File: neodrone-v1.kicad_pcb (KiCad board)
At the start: 4 copper layers, 150 x 105 mm, 39 parts, among them J1 Conn_01x05_Socket, U1 ATSAMD21G18A-A, U2 MPU-6000

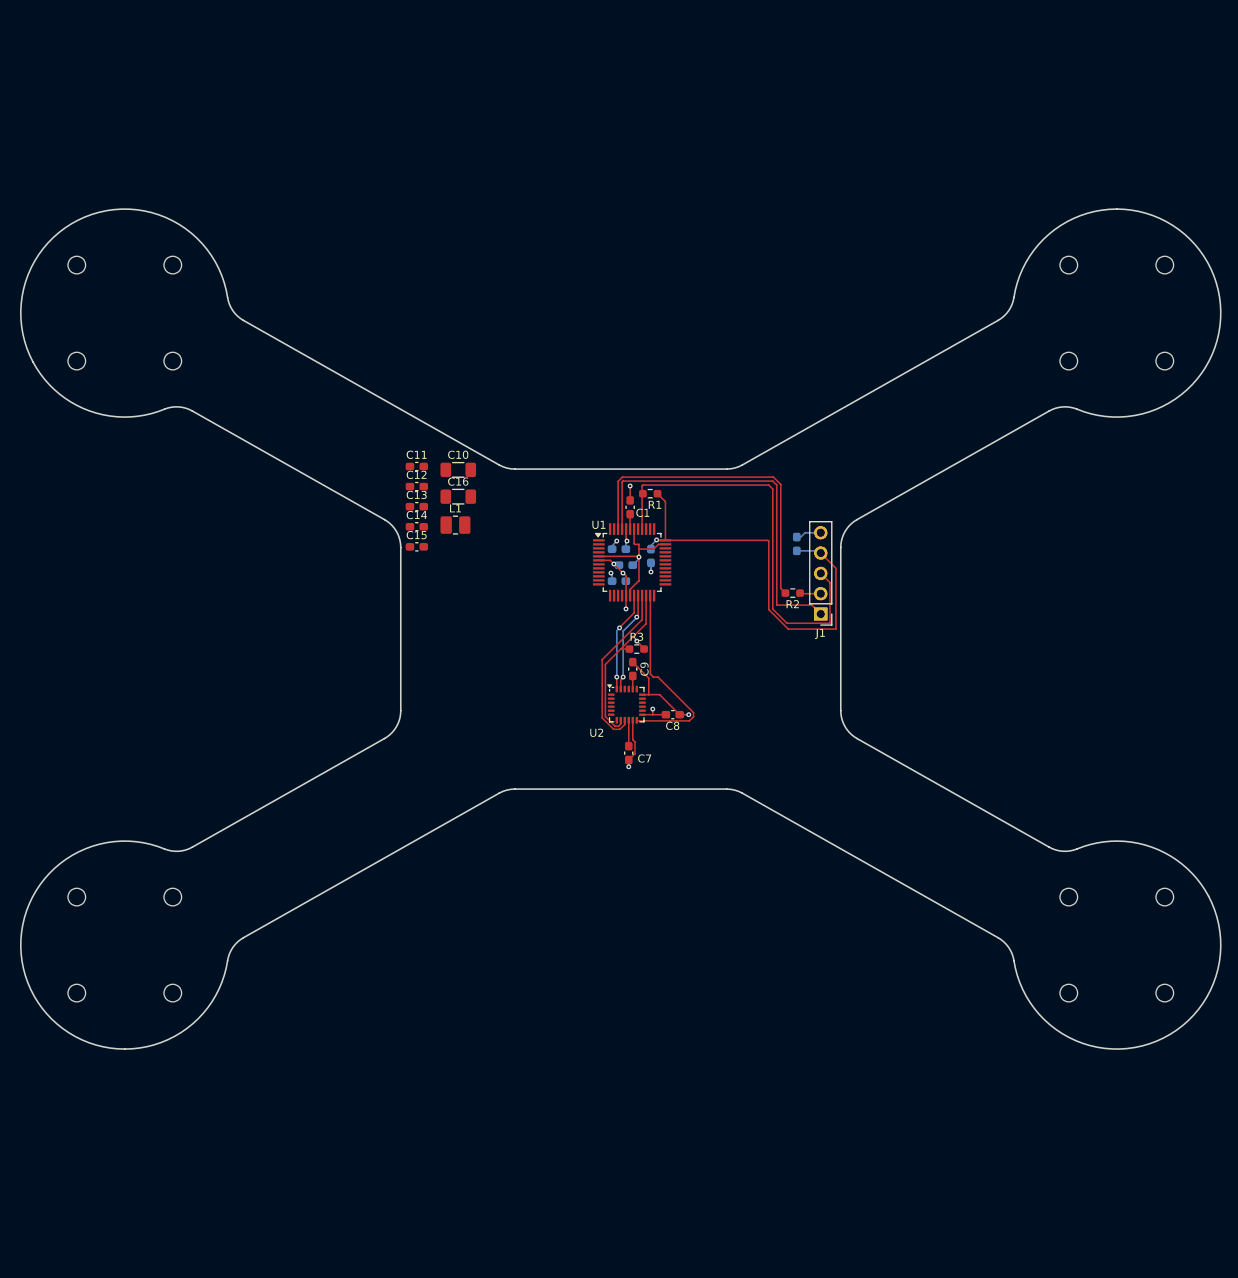
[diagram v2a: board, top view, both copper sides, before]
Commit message: Schematics mostly done, netclasses, coords for esc (angled)
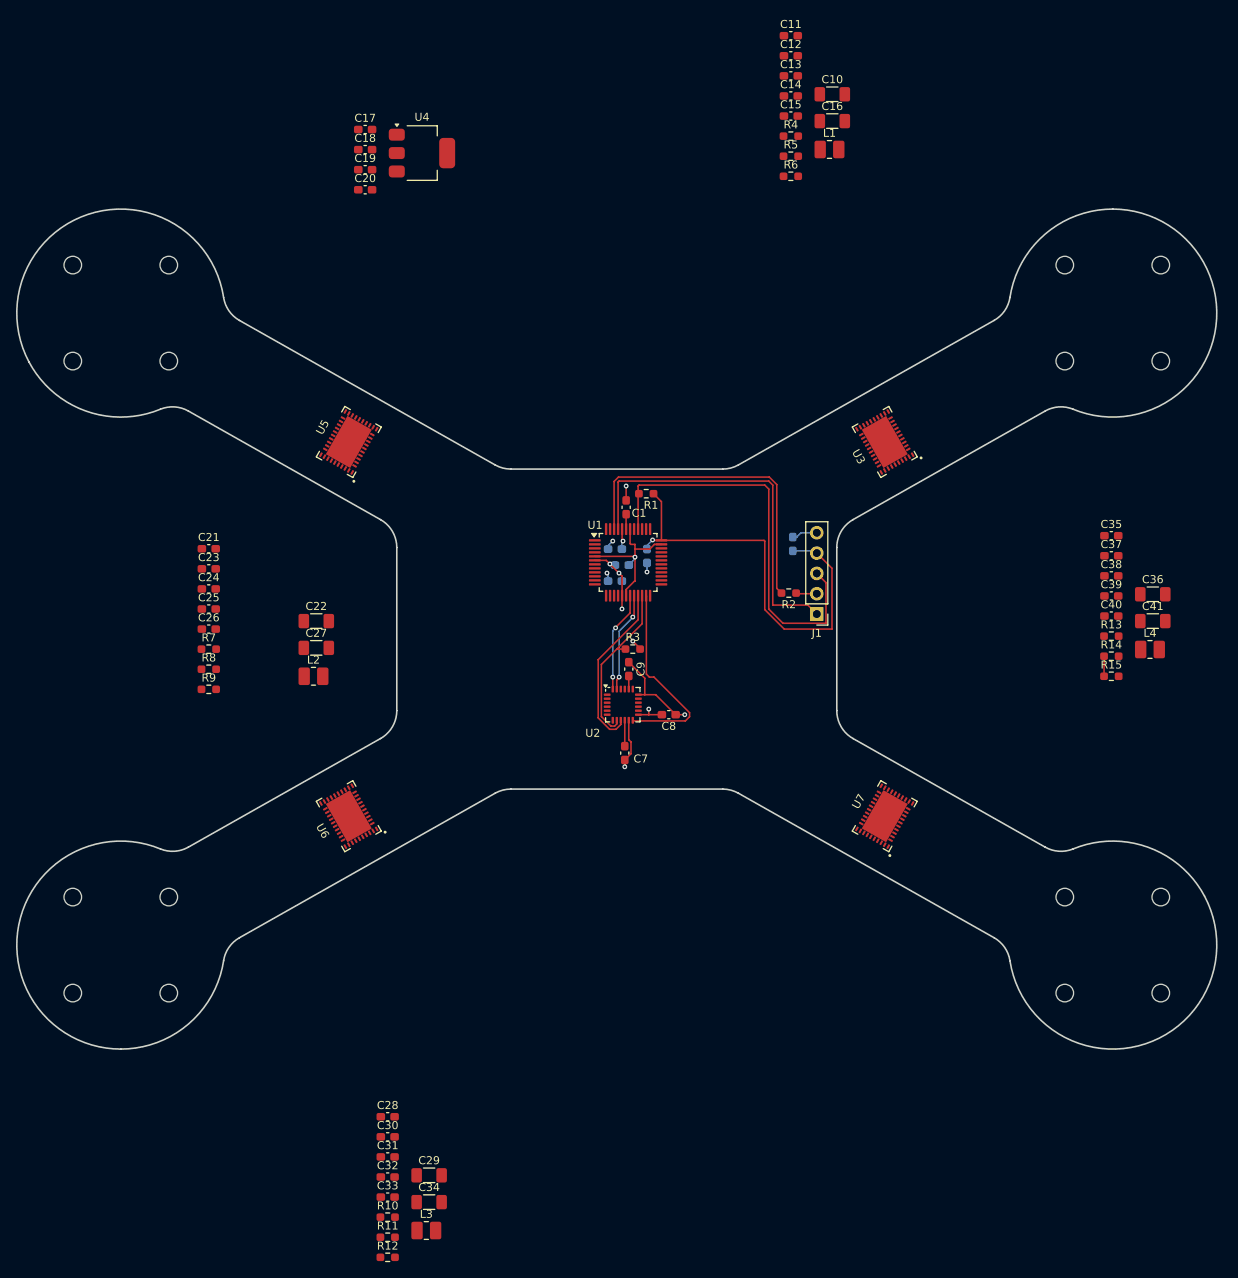
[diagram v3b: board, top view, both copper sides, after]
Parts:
- added C17: 100nF, Capacitor_SMD:C_0603_1608Metric_Pad1.08x0.95mm_HandSolder, F.Cu at (118.5, 37.6)
- added C18: 10uF, Capacitor_SMD:C_0603_1608Metric_Pad1.08x0.95mm_HandSolder, F.Cu at (118.5, 40.1)
- added C19: 100nF, Capacitor_SMD:C_0603_1608Metric_Pad1.08x0.95mm_HandSolder, F.Cu at (118.5, 42.6)
- added C20: 10uF, Capacitor_SMD:C_0603_1608Metric_Pad1.08x0.95mm_HandSolder, F.Cu at (118.5, 45.1)
- added C21: 100nF, Capacitor_SMD:C_0603_1608Metric_Pad1.08x0.95mm_HandSolder, F.Cu at (99.0, 90.0)
- added C22: 22uF, Capacitor_SMD:C_1206_3216Metric_Pad1.33x1.80mm_HandSolder, F.Cu at (112.4, 99.0)
- added C23: 1uF, Capacitor_SMD:C_0603_1608Metric_Pad1.08x0.95mm_HandSolder, F.Cu at (99.0, 92.5)
- added C24: 1uF, Capacitor_SMD:C_0603_1608Metric_Pad1.08x0.95mm_HandSolder, F.Cu at (99.0, 95.0)
- added C25: 1uF, Capacitor_SMD:C_0603_1608Metric_Pad1.08x0.95mm_HandSolder, F.Cu at (99.0, 97.5)
- added C26: 47nF, Capacitor_SMD:C_0603_1608Metric_Pad1.08x0.95mm_HandSolder, F.Cu at (99.0, 100.0)
- added C27: 22uF, Capacitor_SMD:C_1206_3216Metric_Pad1.33x1.80mm_HandSolder, F.Cu at (112.4, 102.3)
- added C28: 100nF, Capacitor_SMD:C_0603_1608Metric_Pad1.08x0.95mm_HandSolder, F.Cu at (121.4, 161.0)
- added C29: 22uF, Capacitor_SMD:C_1206_3216Metric_Pad1.33x1.80mm_HandSolder, F.Cu at (126.5, 168.3)
- added C30: 1uF, Capacitor_SMD:C_0603_1608Metric_Pad1.08x0.95mm_HandSolder, F.Cu at (121.4, 163.5)
- added C31: 1uF, Capacitor_SMD:C_0603_1608Metric_Pad1.08x0.95mm_HandSolder, F.Cu at (121.4, 166.0)
- added C32: 1uF, Capacitor_SMD:C_0603_1608Metric_Pad1.08x0.95mm_HandSolder, F.Cu at (121.4, 168.5)
- added C33: 47nF, Capacitor_SMD:C_0603_1608Metric_Pad1.08x0.95mm_HandSolder, F.Cu at (121.4, 171.0)
- added C34: 22uF, Capacitor_SMD:C_1206_3216Metric_Pad1.33x1.80mm_HandSolder, F.Cu at (126.5, 171.6)
- added C35: 100nF, Capacitor_SMD:C_0603_1608Metric_Pad1.08x0.95mm_HandSolder, F.Cu at (211.8, 88.3)
- added C36: 22uF, Capacitor_SMD:C_1206_3216Metric_Pad1.33x1.80mm_HandSolder, F.Cu at (217.0, 95.7)
- added C37: 1uF, Capacitor_SMD:C_0603_1608Metric_Pad1.08x0.95mm_HandSolder, F.Cu at (211.8, 90.8)
- added C38: 1uF, Capacitor_SMD:C_0603_1608Metric_Pad1.08x0.95mm_HandSolder, F.Cu at (211.8, 93.3)
- added C39: 1uF, Capacitor_SMD:C_0603_1608Metric_Pad1.08x0.95mm_HandSolder, F.Cu at (211.8, 95.9)
- added C40: 47nF, Capacitor_SMD:C_0603_1608Metric_Pad1.08x0.95mm_HandSolder, F.Cu at (211.8, 98.4)
- added C41: 22uF, Capacitor_SMD:C_1206_3216Metric_Pad1.33x1.80mm_HandSolder, F.Cu at (217.0, 99.0)
- added L2: 2.2uH, Inductor_SMD:L_1008_2520Metric_Pad1.43x2.20mm_HandSolder, F.Cu at (112.1, 105.9)
- added L3: 2.2uH, Inductor_SMD:L_1008_2520Metric_Pad1.43x2.20mm_HandSolder, F.Cu at (126.2, 175.2)
- added L4: 2.2uH, Inductor_SMD:L_1008_2520Metric_Pad1.43x2.20mm_HandSolder, F.Cu at (216.7, 102.5)
- added R10: 10k, Resistor_SMD:R_0603_1608Metric_Pad0.98x0.95mm_HandSolder, F.Cu at (121.4, 173.5)
- added R11: 10k, Resistor_SMD:R_0603_1608Metric_Pad0.98x0.95mm_HandSolder, F.Cu at (121.4, 176.0)
- added R12: 10k, Resistor_SMD:R_0603_1608Metric_Pad0.98x0.95mm_HandSolder, F.Cu at (121.4, 178.5)
- added R13: 10k, Resistor_SMD:R_0603_1608Metric_Pad0.98x0.95mm_HandSolder, F.Cu at (211.8, 100.9)
- added R14: 10k, Resistor_SMD:R_0603_1608Metric_Pad0.98x0.95mm_HandSolder, F.Cu at (211.8, 103.4)
- added R15: 10k, Resistor_SMD:R_0603_1608Metric_Pad0.98x0.95mm_HandSolder, F.Cu at (211.8, 105.9)
- added R4: 10k, Resistor_SMD:R_0603_1608Metric_Pad0.98x0.95mm_HandSolder, F.Cu at (171.8, 38.4)
- added R5: 10k, Resistor_SMD:R_0603_1608Metric_Pad0.98x0.95mm_HandSolder, F.Cu at (171.8, 40.9)
- added R6: 10k, Resistor_SMD:R_0603_1608Metric_Pad0.98x0.95mm_HandSolder, F.Cu at (171.8, 43.4)
- added R7: 10k, Resistor_SMD:R_0603_1608Metric_Pad0.98x0.95mm_HandSolder, F.Cu at (99.0, 102.5)
- added R8: 10k, Resistor_SMD:R_0603_1608Metric_Pad0.98x0.95mm_HandSolder, F.Cu at (99.0, 105.0)
- added R9: 10k, Resistor_SMD:R_0603_1608Metric_Pad0.98x0.95mm_HandSolder, F.Cu at (99.0, 107.5)
- added U3: MCF8316A, MCF8316:MCF8316A_RGF0040E_VQFN-40-1EP_7x5mm_P0.5mm_EP5.5x3.5mm_kicad5_fixed_rotation, F.Cu at (183.5, 76.6)
- added U4: MCP1826S, Package_TO_SOT_SMD:SOT-223-3_TabPin2, F.Cu at (125.7, 40.5)
- added U5: MCF8316A, MCF8316:MCF8316A_RGF0040E_VQFN-40-1EP_7x5mm_P0.5mm_EP5.5x3.5mm_kicad5_fixed_rotation, F.Cu at (116.5, 76.6)
- added U6: MCF8316A, MCF8316:MCF8316A_RGF0040E_VQFN-40-1EP_7x5mm_P0.5mm_EP5.5x3.5mm_kicad5_fixed_rotation, F.Cu at (116.5, 123.4)
- added U7: MCF8316A, MCF8316:MCF8316A_RGF0040E_VQFN-40-1EP_7x5mm_P0.5mm_EP5.5x3.5mm_kicad5_fixed_rotation, F.Cu at (183.5, 123.4)
- moved C11 71.3 mm to (171.8, 25.8)
- moved C13 71.3 mm to (171.8, 30.9)
- moved C15 71.3 mm to (171.8, 35.9)
- moved C12 71.3 mm to (171.8, 28.3)
- moved C14 71.3 mm to (171.8, 33.4)
- moved C10 66.3 mm to (176.9, 33.1)
- moved C16 66.3 mm to (176.9, 36.5)
- moved L1 66.3 mm to (176.6, 40.0)
- moved R1 0.50 mm to (153.7, 83.1)
- moved C8 0.50 mm to (156.5, 110.7)
- moved M10 0.50 mm to (82.0, 133.5)
- moved M11 0.50 mm to (82.0, 145.5)
- moved M12 0.50 mm to (94.0, 145.5)
- moved M5 0.50 mm to (94.0, 54.5)
- moved M6 0.50 mm to (82.0, 54.5)
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- renumbered REF** to M1, REF** to M10, REF** to M11, REF** to M12, REF** to M13, REF** to M14, REF** to M15, REF** to M16, REF** to M2, REF** to M3, REF** to M4, REF** to M5, REF** to M6, REF** to M7, REF** to M8, REF** to M9
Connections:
- net /motor_esc/PGND_M1 renamed /motor_esc1/PGND_M1
- net /motor_esc/VBAT renamed /motor_esc1/VBAT
- net /motor_esc/VBK_M1 renamed VBK_M1
- C16 pad 2: /motor_esc/GND_BK_M1 -> GND_BK_M1
- U1 pad 13: /mcu/I2C_SDA -> unconnected-(U1-PA08-Pad13)
- U1 pad 14: /mcu/I2C_SCL -> unconnected-(U1-PA09-Pad14)
- U1 pad 25: /mcu/M1_PWM -> M1_PWM
- U1 pad 26: /mcu/M2_PWM -> M2_PWM
- U1 pad 27: /mcu/M3_PWM -> M3_PWM
- U1 pad 28: /mcu/M4_PWM -> M4_PWM
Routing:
- net Net-(U7-AGND): track 0.00 -> 2.51 mm
- net +3V3: track 93.5 -> 95.1 mm
- net GND: track 45.7 -> 46.9 mm

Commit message: A LOT of changes, current state is 2 of 4 ESCs routed, power revamped. \n Board almost done
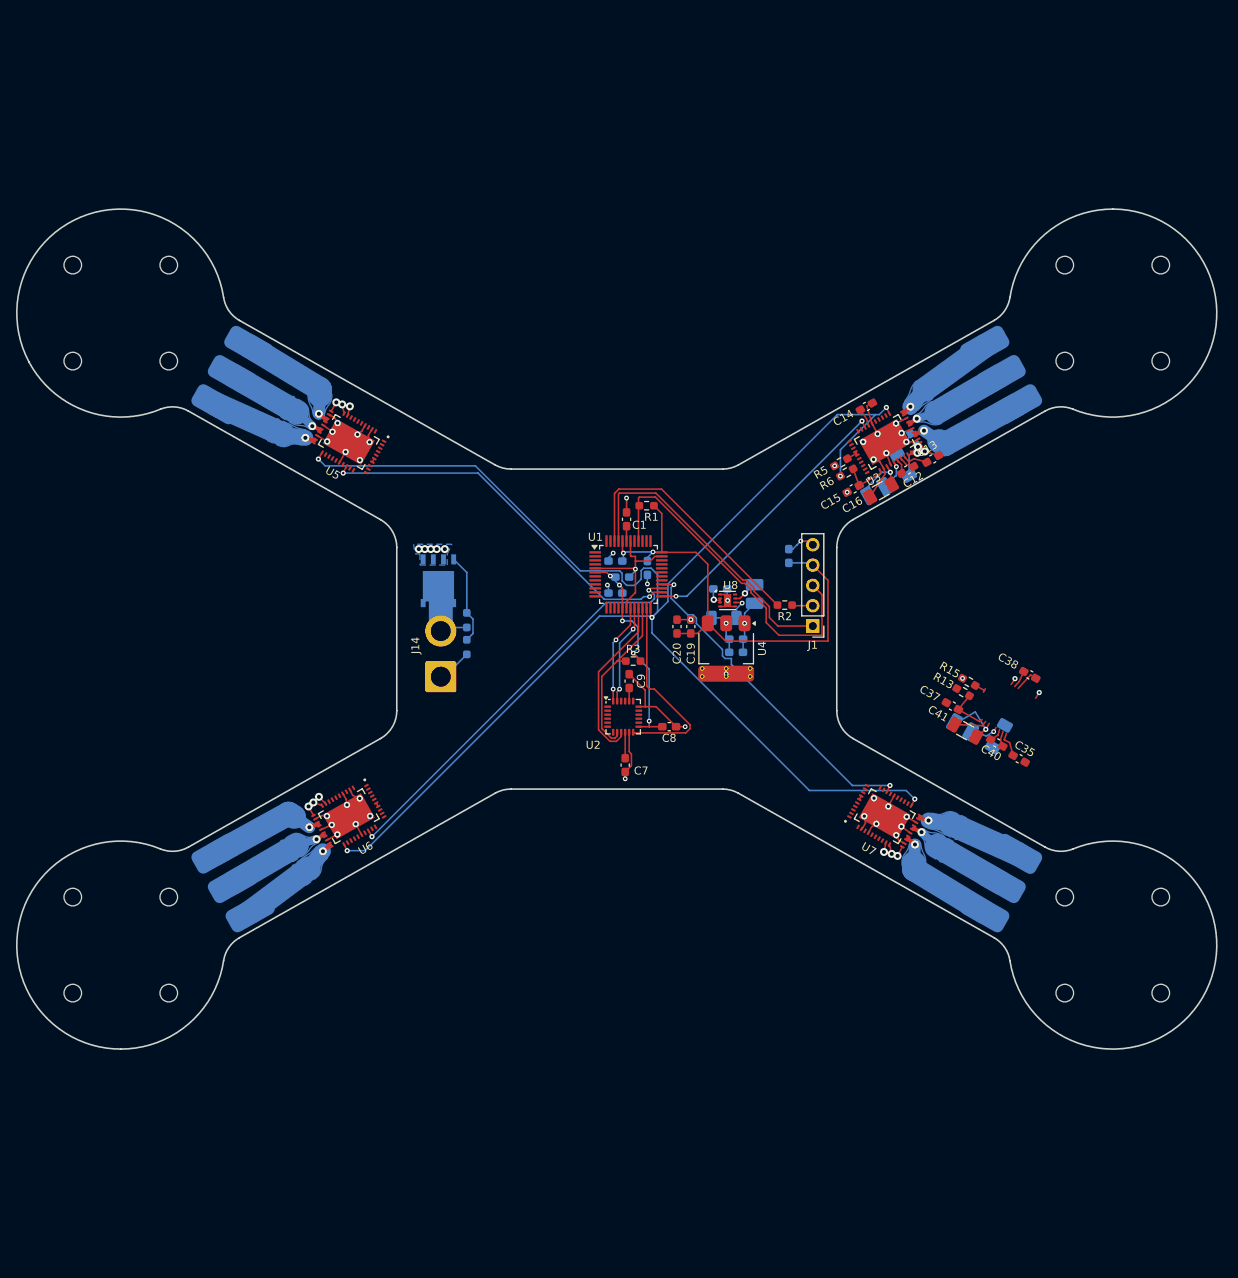
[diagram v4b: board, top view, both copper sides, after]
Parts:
- removed the C10 at (176.9, 33.1)
- removed C21, C28: 100nF, Capacitor_SMD:C_0603_1608Metric_Pad1.08x0.95mm_HandSolder
- removed C22, C27, C29, C34, C36: 22uF, Capacitor_SMD:C_1206_3216Metric_Pad1.33x1.80mm_HandSolder
- removed C23, C24, C25, C30, C31, C32, C39: 1uF, Capacitor_SMD:C_0603_1608Metric_Pad1.08x0.95mm_HandSolder
- removed C26, C33: 47nF, Capacitor_SMD:C_0603_1608Metric_Pad1.08x0.95mm_HandSolder
- removed L2, L3: 2.2uH, Inductor_SMD:L_1008_2520Metric_Pad1.43x2.20mm_HandSolder
- removed R10, R11, R12, R14, R4, R7, R8, R9: 10k, Resistor_SMD:R_0603_1608Metric_Pad0.98x0.95mm_HandSolder
- added C10: 22uF, Capacitor_SMD:C_1206_3216Metric_Pad1.33x1.80mm_HandSolder, B.Cu at (185.8, 79.5)
- added C10: 22uF, Capacitor_SMD:C_1206_3216Metric_Pad1.33x1.80mm_HandSolder, B.Cu at (197.7, 113.4)
- added C42: 10uF, Capacitor_SMD:C_0603_1608Metric_Pad1.08x0.95mm_HandSolder, B.Cu at (162.9, 95.0)
- added C43: 22uF, Capacitor_SMD:C_1206_3216Metric_Pad1.33x1.80mm_HandSolder, B.Cu at (163.4, 98.6)
- added J10: SolderWirePad_1x01_SMD_3x6mm, Connector_Wire:SolderWirePad_1x01_SMD_3x6mm, B.Cu at (104.2, 135.4)
- added J11: SolderWirePad_1x01_SMD_3x6mm, Connector_Wire:SolderWirePad_1x01_SMD_3x6mm, B.Cu at (196.0, 135.4)
- added J12: SolderWirePad_1x01_SMD_3x6mm, Connector_Wire:SolderWirePad_1x01_SMD_3x6mm, B.Cu at (198.1, 131.8)
- added J13: SolderWirePad_1x01_SMD_3x6mm, Connector_Wire:SolderWirePad_1x01_SMD_3x6mm, B.Cu at (200.1, 128.1)
- added J14: Conn_01x02, Connector_Wire:SolderWire-2sqmm_1x02_P7.8mm_D2mm_OD3.9mm, F.Cu at (128.0, 106.0)
- added J2: SolderWirePad_1x01_SMD_3x6mm, Connector_Wire:SolderWirePad_1x01_SMD_3x6mm, B.Cu at (200.1, 71.9)
- added J3: SolderWirePad_1x01_SMD_3x6mm, Connector_Wire:SolderWirePad_1x01_SMD_3x6mm, B.Cu at (198.1, 68.2)
- added J4: SolderWirePad_1x01_SMD_3x6mm, Connector_Wire:SolderWirePad_1x01_SMD_3x6mm, B.Cu at (196.0, 64.6)
- added J5: SolderWirePad_1x01_SMD_3x6mm, Connector_Wire:SolderWirePad_1x01_SMD_3x6mm, B.Cu at (104.0, 64.6)
- added J6: SolderWirePad_1x01_SMD_3x6mm, Connector_Wire:SolderWirePad_1x01_SMD_3x6mm, B.Cu at (102.0, 68.2)
- added J7: SolderWirePad_1x01_SMD_3x6mm, Connector_Wire:SolderWirePad_1x01_SMD_3x6mm, B.Cu at (99.9, 71.9)
- added J8: SolderWirePad_1x01_SMD_3x6mm, Connector_Wire:SolderWirePad_1x01_SMD_3x6mm, B.Cu at (99.9, 128.1)
- added J9: SolderWirePad_1x01_SMD_3x6mm, Connector_Wire:SolderWirePad_1x01_SMD_3x6mm, B.Cu at (102.0, 131.8)
- added L5: 2.2uH, Inductor_SMD:L_1008_2520Metric_Pad1.43x2.20mm_HandSolder, B.Cu at (167.2, 95.6)
- added Q1: Si7139DP, Package_SO:PowerPAK_SO-8_Single, B.Cu at (127.7, 94.0)
- added R16: 100k, Resistor_SMD:R_0603_1608Metric_Pad0.98x0.95mm_HandSolder, B.Cu at (131.2, 98.9)
- added R17: 100k, Resistor_SMD:R_0603_1608Metric_Pad0.98x0.95mm_HandSolder, B.Cu at (131.2, 102.2)
- added U8: TPS62163DSG, Package_SON:WSON-8-1EP_2x2mm_P0.5mm_EP0.9x1.6mm, F.Cu at (163.8, 96.4)
- C11, C17, C18, L1, L4: moved to B.Cu
- C35: value 100nF -> 1uF
- U3, U5, U6, U7: footprint MCF8316:MCF8316A_RGF0040E_VQFN-40-1EP_7x5mm_P0.5mm_EP5.5x3.5mm_kicad5_fixed_rotation -> MCF8316:MCF8316A_RGF0040E_VQFN-40-1EP_7x5mm_P0.5mm_EP5.5x3.5mm
- moved C17 78.8 mm to (164.9, 101.2), turned to 180 degrees
- moved C18 78.1 mm to (164.9, 102.9)
- moved U4 72.7 mm to (163.7, 102.4), turned to -90 degrees
- moved C19 70.1 mm to (159.2, 99.7), turned to 90 degrees
- moved C20 67.1 mm to (157.5, 99.7), turned to -90 degrees
- moved C12 53.8 mm to (186.3, 80.1), turned to -150.524 degrees
- moved C11 52.8 mm to (187.2, 76.3), turned to 119.476 degrees
- moved C13 51.1 mm to (189.5, 78.7), turned to 29.476 degrees
- moved C15 47.3 mm to (179.6, 82.5), turned to -150.524 degrees
- moved C16 46.6 mm to (183.0, 82.7), turned to -150.524 degrees
- moved L1 43.1 mm to (182.5, 82.8), turned to -150.524 degrees
- moved C14 39.9 mm to (181.2, 72.2), turned to 29.476 degrees
- moved R5 38.8 mm to (178.0, 79.2), turned to 29.476 degrees
- moved R6 37.7 mm to (178.8, 80.4), turned to -150.524 degrees
- moved C35 30.2 mm to (200.3, 116.2), turned to -29.4758 degrees
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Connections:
- C11 pad 1: /motor_esc1/VBAT -> VBAT
- C11 pad 2: /motor_esc1/PGND_M1 -> GND
- C13 pad 2: /motor_esc1/VBAT -> VBAT
- C14 pad 2: Net-(U3-AGND) -> GND
- C15 pad 2: Net-(U3-DGND) -> GND
- C16 pad 2: GND_BK_M1 -> GND
- C17 pad 1: VBK_M1 -> Net-(U4-VI)
- C17 pad 2: GND_BK_M1 -> GND
- C18 pad 1: GND_BK_M1 -> GND
- C18 pad 2: VBK_M1 -> Net-(U4-VI)
- C19 pad 2: GND_BK_M1 -> GND
- C20 pad 1: GND_BK_M1 -> GND
- C35 pad 1: /motor_esc4/VBAT -> Net-(U3-CP)
- C35 pad 2: /motor_esc4/PGND_M4 -> VBAT
- C37 pad 1: Net-(U7-DVDD) -> Net-(U3-DVDD)
- C37 pad 2: Net-(U7-DGND) -> GND
- C38 pad 1: Net-(U7-AVDD) -> Net-(U3-AVDD)
- C38 pad 2: Net-(U7-AGND) -> GND
- C40 pad 1: Net-(U7-CPH) -> Net-(U3-CPH)
- C40 pad 2: Net-(U7-CPL) -> Net-(U3-CPL)
- C41 pad 2: GND_BK_M4 -> GND
- R13 pad 1: Net-(U7-AVDD) -> Net-(U3-DVDD)
- R15 pad 1: Net-(U7-AGND) -> GND
- R15 pad 2: Net-(U7-BRAKE) -> Net-(U3-BRAKE)
- R5 pad 1: Net-(U3-AGND) -> GND
- R6 pad 1: Net-(U3-AVDD) -> Net-(U3-DVDD)
- U1 pad 24: unconnected-(U1-PA15-Pad24) -> DRVOFF_ALL
- U3 pad 10: /motor_esc1/VBAT -> VBAT
- U3 pad 11: /motor_esc1/VBAT -> VBAT
- U3 pad 12: /motor_esc1/PGND_M1 -> GND
- U3 pad 15: /motor_esc1/PGND_M1 -> GND
- U3 pad 18: /motor_esc1/PGND_M1 -> GND
- U3 pad 2: Net-(U3-DGND) -> GND
- U3 pad 26: Net-(U3-AGND) -> GND
- U3 pad 34: Net-(U3-DIR) -> Net-(U3-BRAKE)
- U3 pad 4: GND_BK_M1 -> GND
- U3 pad 41: /motor_esc1/PGND_M1 -> GND
- U3 pad 9: /motor_esc1/VBAT -> VBAT
- U4 pad 1: VBK_M1 -> Net-(U4-VI)
- U4 pad 2: GND_BK_M1 -> GND
- U5 pad 10: /motor_esc2/VBAT -> VBAT
- U5 pad 11: /motor_esc2/VBAT -> VBAT
- U5 pad 12: /motor_esc2/PGND_M2 -> GND
- U5 pad 15: /motor_esc2/PGND_M2 -> GND
- U5 pad 18: /motor_esc2/PGND_M2 -> GND
- U5 pad 2: Net-(U5-DGND) -> GND
- U5 pad 26: Net-(U5-AGND) -> GND
- U5 pad 34: Net-(U5-DIR) -> Net-(U5-BRAKE)
- U5 pad 4: GND_BK_M2 -> GND
- U5 pad 41: /motor_esc2/PGND_M2 -> GND
- U5 pad 9: /motor_esc2/VBAT -> VBAT
- U6 pad 10: /motor_esc3/VBAT -> VBAT
- U6 pad 11: /motor_esc3/VBAT -> VBAT
- U6 pad 12: /motor_esc3/PGND_M3 -> GND
- U6 pad 15: /motor_esc3/PGND_M3 -> GND
- U6 pad 18: /motor_esc3/PGND_M3 -> GND
- U6 pad 2: Net-(U6-DGND) -> GND
- U6 pad 26: Net-(U6-AGND) -> GND
- U6 pad 34: Net-(U6-DIR) -> Net-(U6-BRAKE)
- U6 pad 4: GND_BK_M3 -> GND
- U6 pad 41: /motor_esc3/PGND_M3 -> GND
- U6 pad 9: /motor_esc3/VBAT -> VBAT
- U7 pad 10: /motor_esc4/VBAT -> VBAT
- U7 pad 11: /motor_esc4/VBAT -> VBAT
- U7 pad 12: /motor_esc4/PGND_M4 -> GND
- U7 pad 15: /motor_esc4/PGND_M4 -> GND
- U7 pad 18: /motor_esc4/PGND_M4 -> GND
- U7 pad 2: Net-(U7-DGND) -> GND
- U7 pad 26: Net-(U7-AGND) -> GND
- U7 pad 34: Net-(U7-DIR) -> Net-(U7-BRAKE)
- U7 pad 4: GND_BK_M4 -> GND
- U7 pad 41: /motor_esc4/PGND_M4 -> GND
- U7 pad 9: /motor_esc4/VBAT -> VBAT
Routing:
- net DRVOFF_ALL: track 0.00 -> 207.4 mm, vias 0 -> 7
- net GND: track 46.9 -> 132.3 mm, vias 8 -> 43
- net M3_PWM: track 0.00 -> 51.6 mm, vias 0 -> 2
- net M2_PWM: track 0.00 -> 47.7 mm, vias 0 -> 2
- net M4_PWM: track 0.00 -> 43.5 mm, vias 0 -> 3
- net M1_PWM: track 0.00 -> 35.0 mm, vias 0 -> 2
- net VBAT: track 0.00 -> 24.1 mm, vias 0 -> 18
- net /motor_esc2/M2_A: track 0.00 -> 15.2 mm, vias 0 -> 1
- net /motor_esc1/M1_A: track 0.00 -> 15.2 mm, vias 0 -> 1
- net /motor_esc3/M3_A: track 0.00 -> 15.1 mm, vias 0 -> 1
- net /motor_esc4/M4_A: track 0.00 -> 15.1 mm, vias 0 -> 1
- net /motor_esc1/M1_C: track 0.00 -> 13.8 mm, vias 0 -> 1
- net /motor_esc2/M2_C: track 0.00 -> 13.7 mm, vias 0 -> 1
- net /motor_esc4/M4_C: track 0.00 -> 13.7 mm, vias 0 -> 1
- net /motor_esc3/M3_C: track 0.00 -> 13.6 mm, vias 0 -> 1
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- added copper zone on B.Cu, net /motor_esc1/M1_B
- added copper zone on B.Cu, net /motor_esc1/M1_C
- added copper zone on B.Cu, net /motor_esc2/M2_A
- added copper zone on B.Cu, net /motor_esc2/M2_B
- added copper zone on B.Cu, net /motor_esc2/M2_C
- added copper zone on B.Cu, net /motor_esc3/M3_B
- added copper zone on B.Cu, net /motor_esc3/M3_C
- added copper zone on B.Cu, net /motor_esc4/M4_A
- added copper zone on B.Cu, net /motor_esc4/M4_B
- added copper zone on B.Cu, net /motor_esc4/M4_C
- added copper zone on B.Cu, net VBAT
- added copper zone on In2.Cu, net VBAT
